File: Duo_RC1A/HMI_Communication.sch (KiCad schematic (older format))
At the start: 27 parts, among them P1 HEADER_180_2.54_10X2, P2 KK3.96_2, U1 SN75176BDR

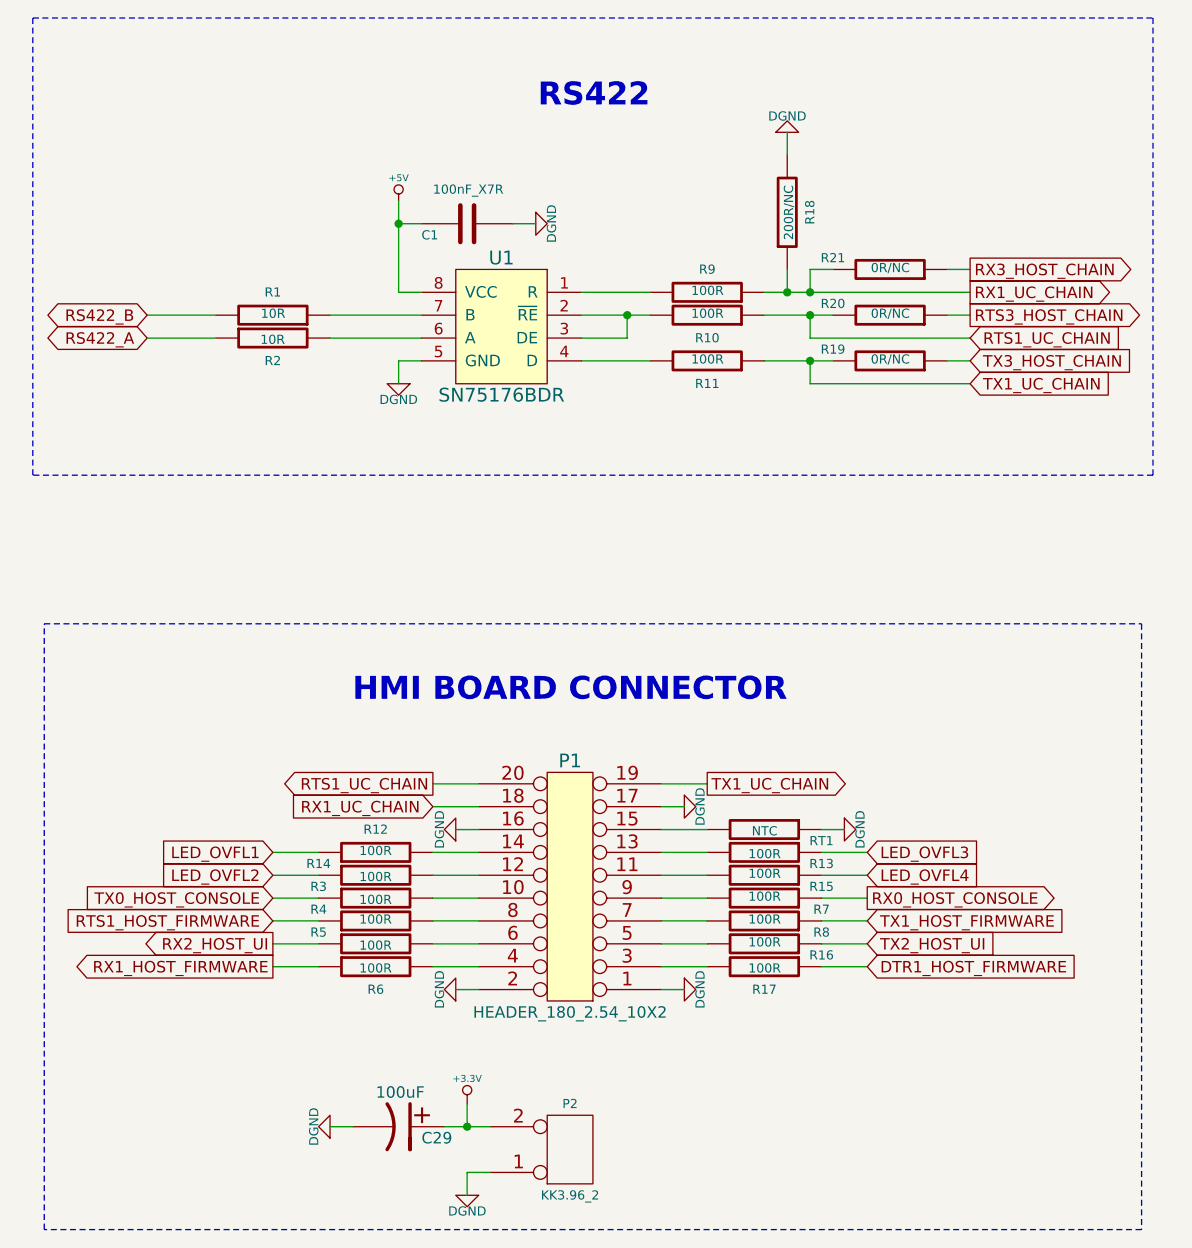
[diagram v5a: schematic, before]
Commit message: Changed the LCD for the 2.8pol. Rotated the bottom board connector. Moved the 3.3V linear regulator from the bottom board to the top board, and changed the power for the top board from 3.3V to 9V.
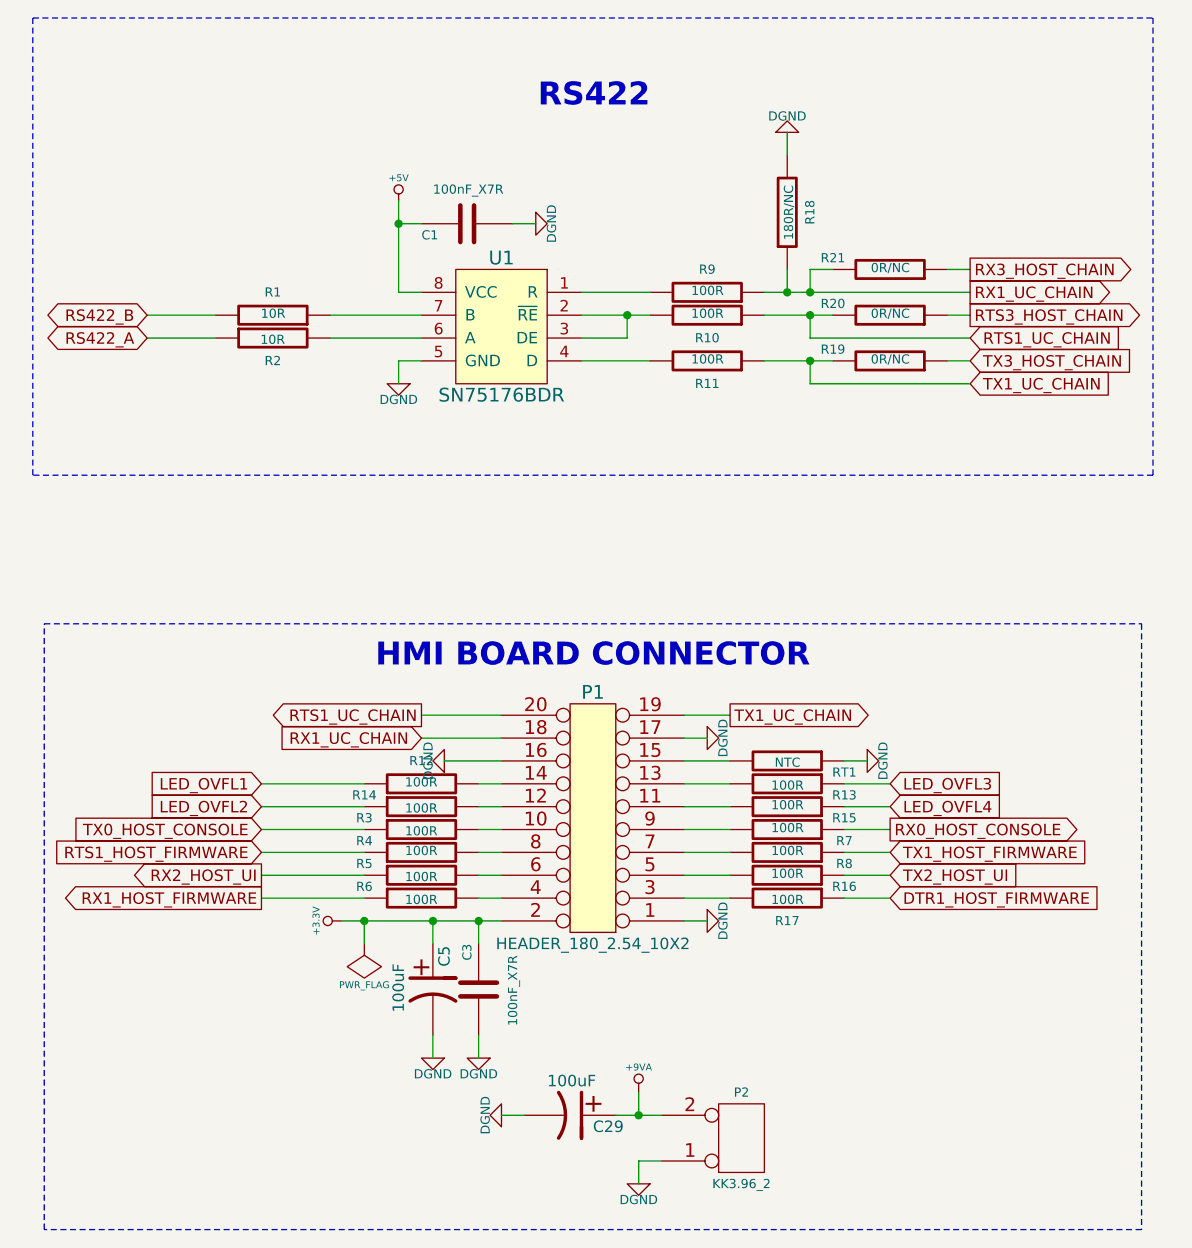
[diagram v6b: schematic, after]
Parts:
- added C3: 100nF_X7R, Duo_Audio_HMI_RC1A:SM0603, symbol C
- added C5: 100uF, Duo_Audio_HMI_RC1A:Capacitor5x11RM2, symbol CP1
- R18: value 200R/NC -> 180R/NC
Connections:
- net +3.3V: now also P1.2 (P2), C3.2, C5.1; no longer C29.1, P2.2 (PM)
- net DGND: now also C3.1, C5.2; no longer P1.2 (P2)
- new net +9VA: C29.1, P2.2 (PM)
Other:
- moved on the sheet: C29, P1, P2, R12, R13, R14, R15, R16, R17, R3, R4, R5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

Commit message: Wrking on the sound. Changed the board size.
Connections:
- net +3.3V: now also P1.1 (P1); no longer P1.2 (P2)
- net DGND: now also P1.14 (P14), P1.2 (P2); no longer P1.1 (P1), P1.16 (P16)
- net RTS1_UC_CHAIN: now also P1.15 (P15); no longer P1.20 (P20)
- net RX1_UC_CHAIN: now also P1.16 (P16); no longer P1.18 (P18)
- net TX1_UC_CHAIN: now also P1.13 (P13); no longer P1.19 (P19)
- net at P1.11 (P11): now also R5.2; no longer R15.2
- net at P1.12 (P12): now also R16.2; no longer R14.2
- net at R13.2: now also P1.19 (P19); no longer P1.13 (P13)
- net at R12.2: now also P1.4 (P4); no longer P1.14 (P14)
- net at RT1.2: now also P1.18 (P18); no longer P1.15 (P15)
- net at P1.3 (P3): now also R4.2; no longer R17.2
- net at R6.2: now also P1.7 (P7); no longer P1.4 (P4)
- net at P1.5 (P5): now also R17.2; no longer R16.2
- net at P1.6 (P6): now also R14.2; no longer R5.2
- net at R8.2: now also P1.8 (P8); no longer P1.7 (P7)
- new net: P1.20 (P20), R15.2
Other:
- moved on the sheet: R12, R13, R14, R15, R16, R17, R3, R4, R5, R6, R7, RT1

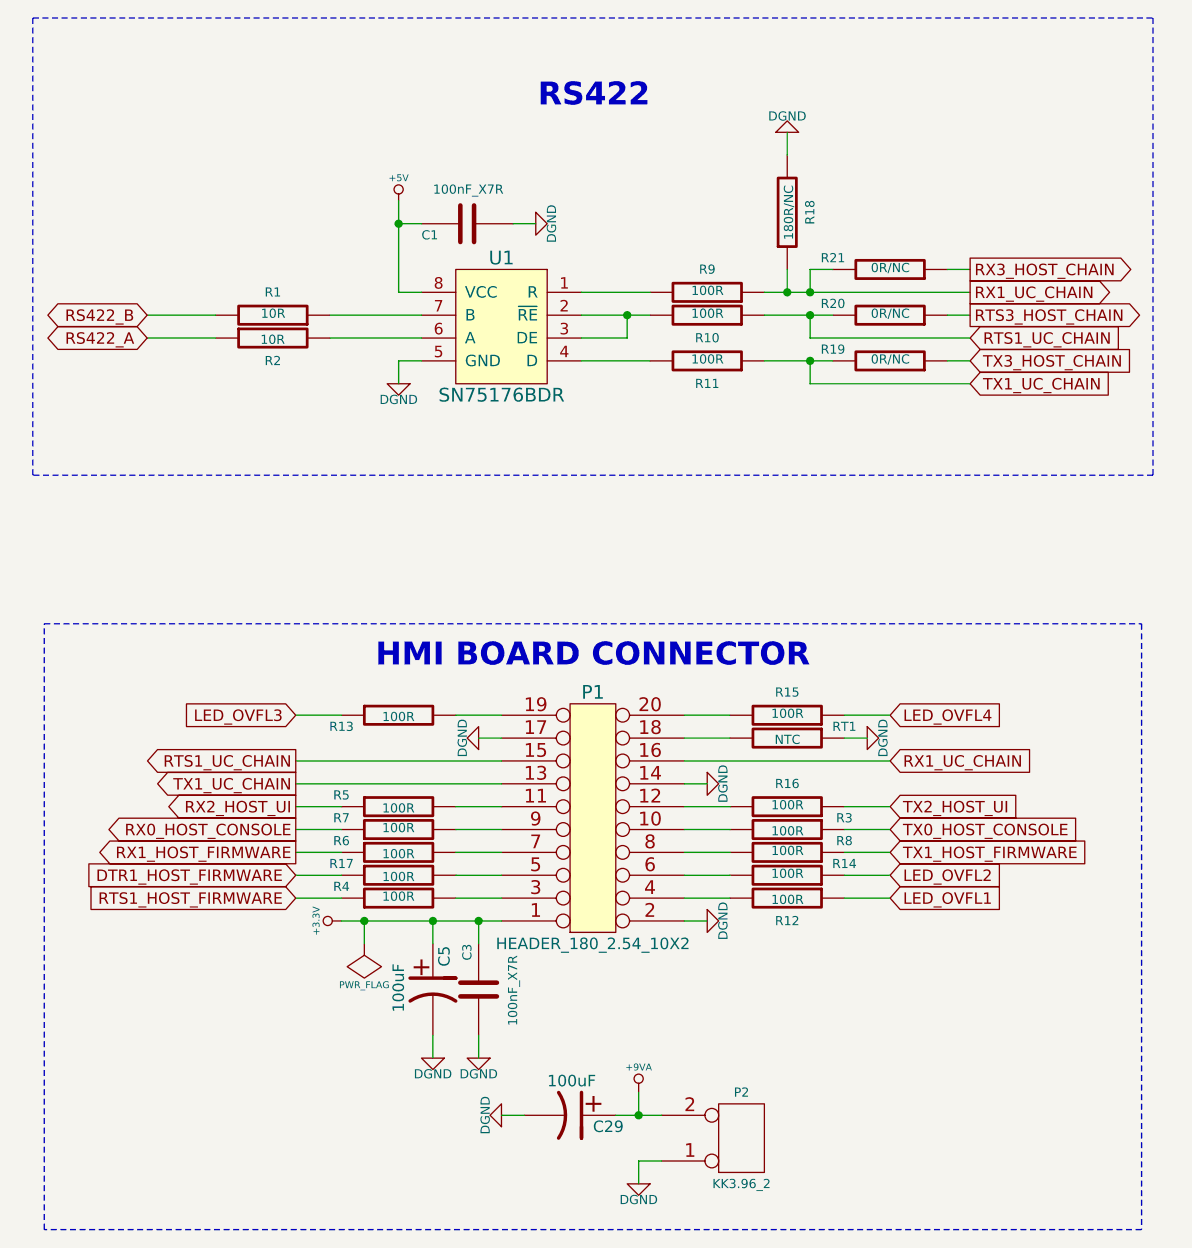
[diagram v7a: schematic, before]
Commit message: USB OTG and HOST traks done.
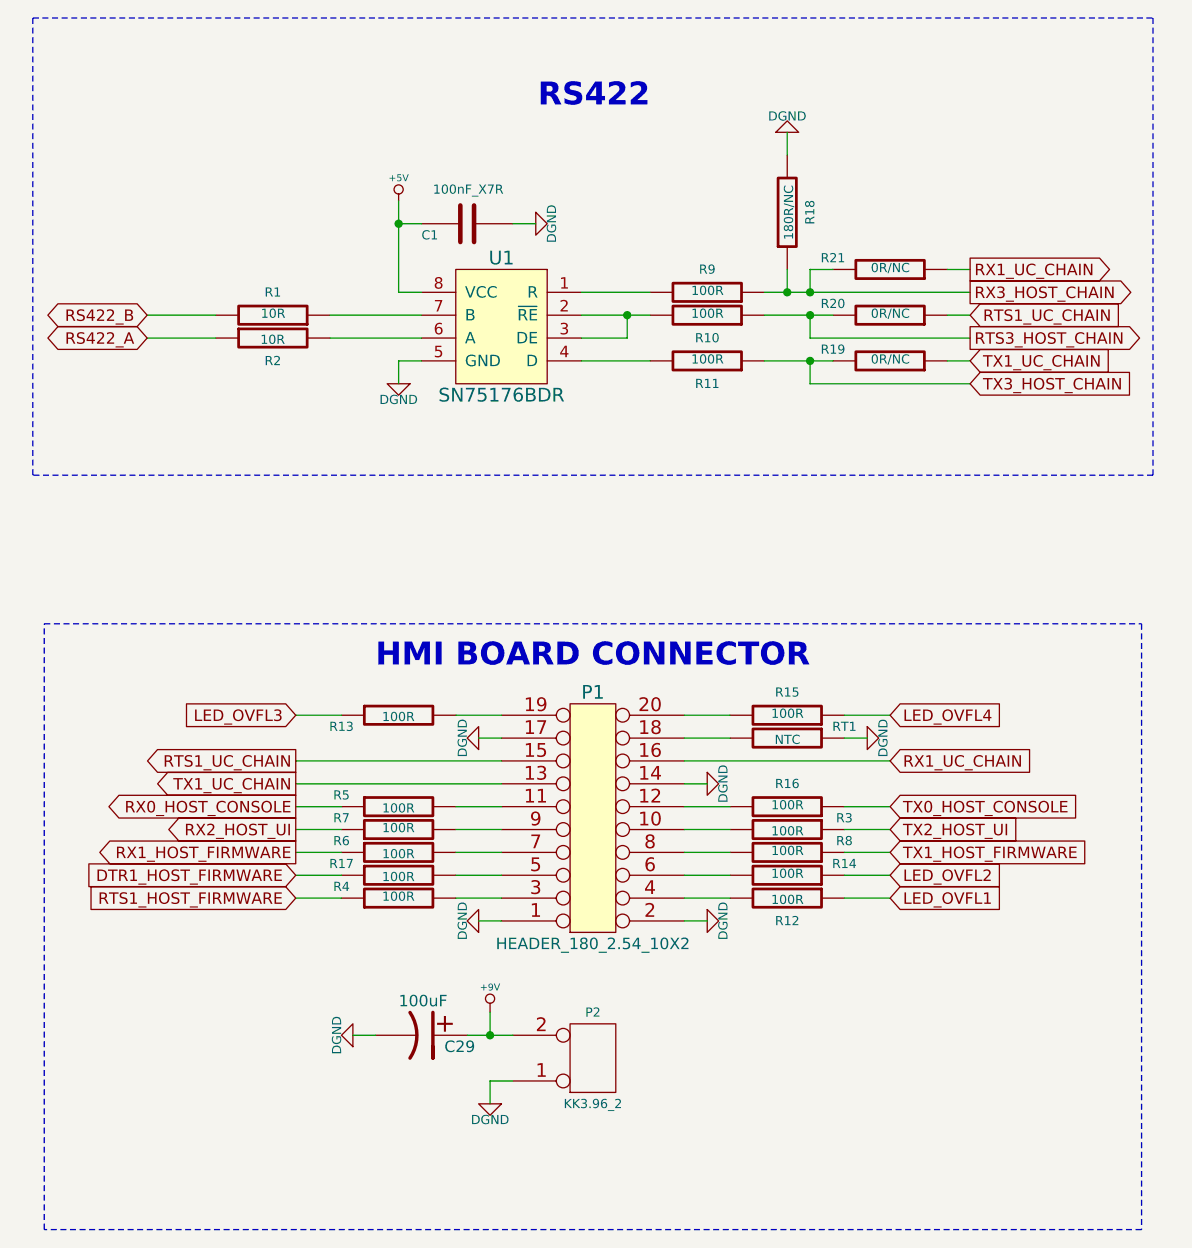
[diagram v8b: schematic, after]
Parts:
- removed C3: 100nF_X7R, Duo_Audio_HMI_RC1A:SM0603, symbol C
- removed C5: 100uF, Duo_Audio_HMI_RC1A:Capacitor5x11RM2, symbol CP1
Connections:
- net +3.3V is gone; now on net DGND: P1.1 (P1)
- net RTS1_UC_CHAIN: now also R20.1; no longer R10.1, R20.2
- net RTS3_HOST_CHAIN: now also R10.1, R20.2; no longer R20.1
- net RX0_HOST_CONSOLE: now also R5.1; no longer R7.1
- net RX1_UC_CHAIN: now also R21.1; no longer R18.1, R21.2, R9.1
- net RX2_HOST_UI: now also R7.1; no longer R5.1
- net RX3_HOST_CHAIN: now also R18.1, R21.2, R9.1; no longer R21.1
- net TX0_HOST_CONSOLE: now also R16.1; no longer R3.1
- net TX1_UC_CHAIN: now also R19.1; no longer R11.1, R19.2
- net TX2_HOST_UI: now also R3.1; no longer R16.1
- net TX3_HOST_CHAIN: now also R11.1, R19.2; no longer R19.1
- net +9VA renamed +9V
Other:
- moved on the sheet: C29, P2
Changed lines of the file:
@@
 	-1   0    0    -1
 $EndComp
-Text GLabel 7200 2350 2    50   Output ~ 0
+Text GLabel 7200 2250 2    50   Output ~ 0
 RX1_UC_CHAIN
-Text GLabel 7200 2550 2    50   Input ~ 0
+Text GLabel 7200 2450 2    50   Input ~ 0
 RTS1_UC_CHAIN
 $Comp
@@
 Text Notes 5800 1550 2    100  ~ 20
 RS422
+Text GLabel 4250 4600 0    50   Output ~ 0
+RX0_HOST_CONSOLE
+Text GLabel 6850 4600 2    50   Input ~ 0
+TX0_HOST_CONSOLE
 Text GLabel 4250 4700 0    50   Output ~ 0
-RX0_HOST_CONSOLE
+RX2_HOST_UI
 Text GLabel 6850 4700 2    50   Input ~ 0
-TX0_HOST_CONSOLE
-Text GLabel 4250 4600 0    50   Output ~ 0
-RX2_HOST_UI
-Text GLabel 6850 4600 2    50   Input ~ 0
 TX2_HOST_UI
 $Comp
@@
 	0    1    -1   0
 $EndComp
-Text GLabel 7200 2750 2    50   Input ~ 0
+Text GLabel 7200 2650 2    50   Input ~ 0
 TX1_UC_CHAIN
 Text GLabel 4250 4900 0    50   Input ~ 0
@@
 Wire Notes Line
 	3100 1150 8000 1150
-Text GLabel 7200 2250 2    50   Output ~ 0
+Text GLabel 7200 2350 2    50   Output ~ 0
 RX3_HOST_CHAIN
-Text GLabel 7200 2450 2    50   Output ~ 0
+Text GLabel 7200 2550 2    50   Output ~ 0
 RTS3_HOST_CHAIN
-Text GLabel 7200 2650 2    50   Input ~ 0
+Text GLabel 7200 2750 2    50   Input ~ 0
 TX3_HOST_CHAIN
 Wire Wire Line
@@
 Wire Wire Line
 	6050 5100 5950 5100
-Wire Wire Line
-	4450 5100 5150 5100
 $Comp
 L CONN_10X2 P1
@@
 L CONN_2 P2
 U 1 1 5383BF02
-P 6200 6050
-F 0 "P2" H 6200 5850 40  0000 C CNN
-F 1 "KK3.96_2" H 6200 6250 40  0000 C CNN
-F 2 "Duo_Audio_HMI_RC1A:KK3.96_2PIN" H 6200 6050 60  0001 C CNN
-F 3 "" H 6200 6050 60  0000 C CNN
-	1    6200 6050
+P 5550 5700
+F 0 "P2" H 5550 5500 40  0000 C CNN
+F 1 "KK3.96_2" H 5550 5900 40  0000 C CNN
+F 2 "Duo_Audio_HMI_RC1A:KK3.96_2PIN" H 5550 5700 60  0001 C CNN
+F 3 "" H 5550 5700 60  0000 C CNN
+	1    5550 5700
 	1    0    0    1
 $EndComp
@@
 L DGND #PWR08
 U 1 1 5383BFC1
-P 5750 6250
-F 0 "#PWR08" H 5750 6250 40  0001 C CNN
-F 1 "DGND" H 5750 6180 40  0000 C CNN
-F 2 "~" H 5750 6250 60  0000 C CNN
-F 3 "~" H 5750 6250 60  0000 C CNN
-	1    5750 6250
+P 5100 5900
+F 0 "#PWR08" H 5100 5900 40  0001 C CNN
+F 1 "DGND" H 5100 5830 40  0000 C CNN
+F 2 "~" H 5100 5900 60  0000 C CNN
+F 3 "~" H 5100 5900 60  0000 C CNN
+	1    5100 5900
 	-1   0    0    -1
 $EndComp
 Wire Wire Line
-	5750 6250 5750 6150
-Wire Wire Line
-	5750 6150 5850 6150
+	5100 5900 5100 5800
+Wire Wire Line
+	5100 5800 5200 5800
 $Comp
 L CP1 C29
 U 1 1 5383CD1B
-P 5450 5950
-F 0 "C29" V 5500 6050 50  0000 L CNN
-F 1 "100uF" V 5300 5850 50  0000 L CNN
-F 2 "Duo_Audio_HMI_RC1A:Capacitor5x11RM2" H 5450 5950 60  0001 C CNN
-F 3 "" H 5450 5950 60  0000 C CNN
-	1    5450 5950
+P 4800 5600
+F 0 "C29" V 4850 5700 50  0000 L CNN
+F 1 "100uF" V 4650 5500 50  0000 L CNN
+F 2 "Duo_Audio_HMI_RC1A:Capacitor5x11RM2" H 4800 5600 60  0001 C CNN
+F 3 "" H 4800 5600 60  0000 C CNN
+	1    4800 5600
 	0    1    1    0
 $EndComp
-Connection ~ 5750 5950
+Connection ~ 5100 5600
 $Comp
 L DGND #PWR09
 U 1 1 5383CE13
-P 5150 5950
-F 0 "#PWR09" H 5150 5950 40  0001 C CNN
-F 1 "DGND" H 5150 5880 40  0000 C CNN
-F 2 "~" H 5150 5950 60  0000 C CNN
-F 3 "~" H 5150 5950 60  0000 C CNN
-	1    5150 5950
-	0    1    -1   0
-$EndComp
-Wire Wire Line
-	5150 5950 5250 5950
+P 4500 5600
+F 0 "#PWR09" H 4500 5600 40  0001 C CNN
+F 1 "DGND" H 4500 5530 40  0000 C CNN
+F 2 "~" H 4500 5600 60  0000 C CNN
+F 3 "~" H 4500 5600 60  0000 C CNN
+	1    4500 5600
+	0    1    -1   0
+$EndComp
+Wire Wire Line
+	4500 5600 4600 5600
 Wire Notes Line
 	7950 3800 7950 6450
@@
 	6650 4300 6750 4300
 Wire Wire Line
-	5650 5950 5850 5950
-Wire Wire Line
-	5750 5850 5750 5950
-$Comp
-L +3.3V #PWR011
-U 1 1 53C5B6BC
-P 4450 5100
-F 0 "#PWR011" H 4450 5060 30  0001 C CNN
-F 1 "+3.3V" H 4450 5210 30  0000 C CNN
-F 2 "" H 4450 5100 60  0000 C CNN
-F 3 "" H 4450 5100 60  0000 C CNN
-	1    4450 5100
-	0    -1   -1   0
-$EndComp
-$Comp
-L +9VA #PWR012
-U 1 1 53C5BF61
-P 5750 5850
-F 0 "#PWR012" H 5750 5820 20  0001 C CNN
-F 1 "+9VA" H 5750 5960 30  0000 C CNN
-F 2 "" H 5750 5850 60  0000 C CNN
-F 3 "" H 5750 5850 60  0000 C CNN
-	1    5750 5850
+	5000 5600 5200 5600
+Wire Wire Line
+	5100 5500 5100 5600
+Wire Wire Line
+	5950 4900 6150 4900
+Wire Wire Line
+	6150 5000 5950 5000
+$Comp
+L DGND #PWR011
+U 1 1 53D0119D
+P 5050 5100
+F 0 "#PWR011" H 5050 5100 40  0001 C CNN
+F 1 "DGND" H 5050 5030 40  0000 C CNN
+F 2 "~" H 5050 5100 60  0000 C CNN
+F 3 "~" H 5050 5100 60  0000 C CNN
+	1    5050 5100
+	0    1    -1   0
+$EndComp
+Wire Wire Line
+	5050 5100 5150 5100
+$Comp
+L +9V #PWR012
+U 1 1 53D06F72
+P 5100 5500
+F 0 "#PWR012" H 5100 5470 20  0001 C CNN
+F 1 "+9V" H 5100 5610 30  0000 C CNN
+F 2 "" H 5100 5500 60  0000 C CNN
+F 3 "" H 5100 5500 60  0000 C CNN
+	1    5100 5500
 	1    0    0    -1
 $EndComp
-$Comp
-L C C3
-U 1 1 53C69F38
-P 5050 5400
-F 0 "C3" V 5000 5200 40  0000 L CNN
-F 1 "100nF_X7R" V 5200 5250 40  0000 L CNN
-F 2 "Duo_Audio_HMI_RC1A:SM0603" H 5088 5250 30  0001 C CNN
-F 3 "~" H 5050 5400 60  0000 C CNN
-	1    5050 5400
-	1    0    0    1
-$EndComp
-Wire Wire Line
-	5050 5200 5050 5100
-Connection ~ 5050 5100
-$Comp
-L DGND #PWR013
-U 1 1 53C69FA8
-P 5050 5700
-F 0 "#PWR013" H 5050 5700 40  0001 C CNN
-F 1 "DGND" H 5050 5630 40  0000 C CNN
-F 2 "~" H 5050 5700 60  0000 C CNN
-F 3 "~" H 5050 5700 60  0000 C CNN
-	1    5050 5700
-	-1   0    0    -1
-$EndComp
-Wire Wire Line
-	5050 5600 5050 5700
-$Comp
-L CP1 C5
-U 1 1 53C6A00E
-P 4850 5400
-F 0 "C5" V 4900 5500 50  0000 L CNN
-F 1 "100uF" V 4700 5300 50  0000 L CNN
-F 2 "Duo_Audio_HMI_RC1A:Capacitor5x11RM2" H 4850 5400 60  0001 C CNN
-F 3 "" H 4850 5400 60  0000 C CNN
-	1    4850 5400
-	1    0    0    -1
-$EndComp
-Wire Wire Line
-	4850 5200 4850 5100
-Connection ~ 4850 5100
-$Comp
-L DGND #PWR014
-U 1 1 53C6A088
-P 4850 5700
-F 0 "#PWR014" H 4850 5700 40  0001 C CNN
-F 1 "DGND" H 4850 5630 40  0000 C CNN
-F 2 "~" H 4850 5700 60  0000 C CNN
-F 3 "~" H 4850 5700 60  0000 C CNN
-	1    4850 5700
-	-1   0    0    -1
-$EndComp
-Wire Wire Line
-	4850 5600 4850 5700
-$Comp
-L PWR_FLAG #FLG015
-U 1 1 53C787C1
-P 4550 5200
-F 0 "#FLG015" H 4550 5295 30  0001 C CNN
-F 1 "PWR_FLAG" H 4550 5380 30  0000 C CNN
-F 2 "" H 4550 5200 60  0000 C CNN
-F 3 "" H 4550 5200 60  0000 C CNN
-	1    4550 5200
-	-1   0    0    1
-$EndComp
-Wire Wire Line
-	4550 5200 4550 5100
-Connection ~ 4550 5100
-Wire Wire Line
-	5950 4900 6150 4900
-Wire Wire Line
-	6150 5000 5950 5000
 $EndSCHEMATC
